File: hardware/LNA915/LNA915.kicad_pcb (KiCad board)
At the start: 4 copper layers, 38 x 7.8 mm, 32 parts, among them P1 HACKRF, P2 ANTENNA, U1 SWITCH, U2 SAW, U3 LNA

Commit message: LNA915 mask clearance fix
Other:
- rule pad_to_mask_clearance: 0.003 -> 0.0762
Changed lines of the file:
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@@
   )
   (setup
-    (last_trace_width 0.24)
+    (last_trace_width 0.1524)
     (user_trace_width 0.2032)
     (user_trace_width 0.24)
@@
     (pad_size 0.762 0.762)
     (pad_drill 0.3048)
-    (pad_to_mask_clearance 0.003)
+    (pad_to_mask_clearance 0.0762)
     (pad_to_paste_clearance_ratio -0.12)
     (aux_axis_origin 0 0)

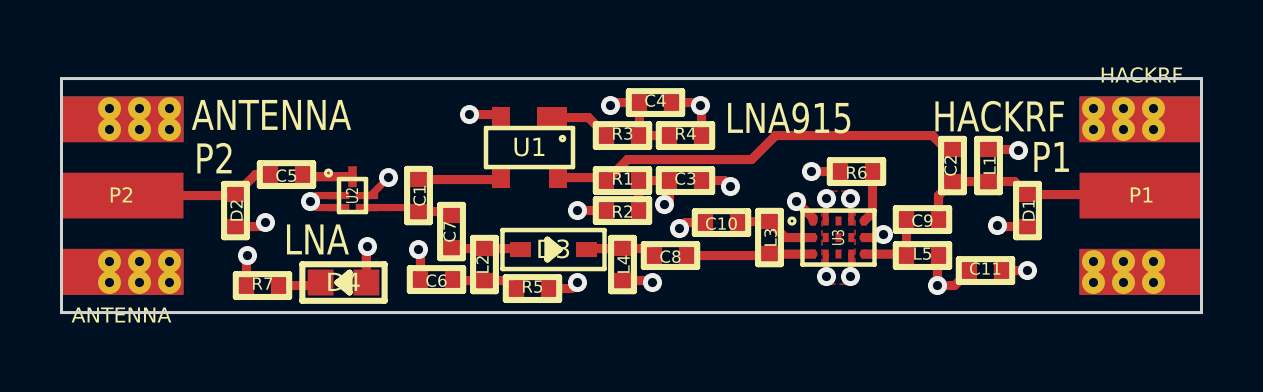
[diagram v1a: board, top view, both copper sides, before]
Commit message: LNA915 grounded mounting holes
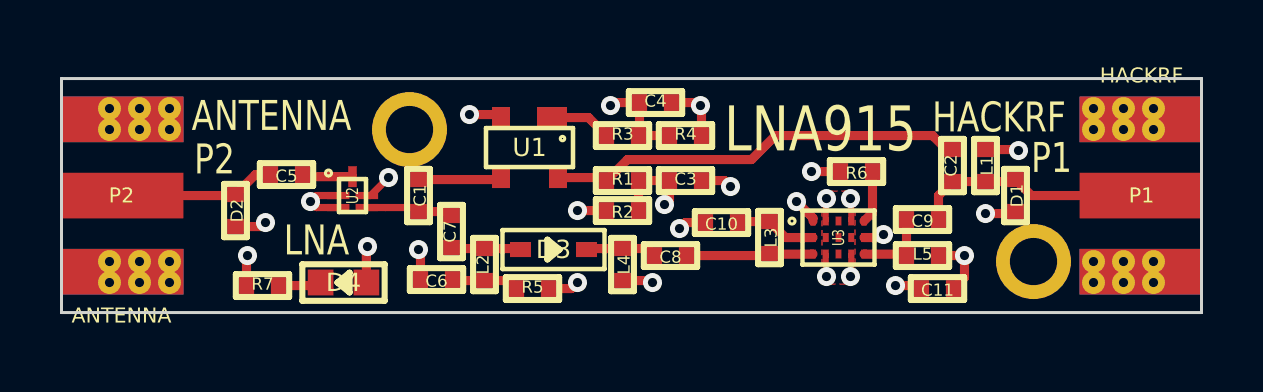
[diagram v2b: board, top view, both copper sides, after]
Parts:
- added P3: CONN_1, GSG-HOLE-62MIL-COPPER, F.Cu at (157.4, 102.2)
- added P4: CONN_1, GSG-HOLE-62MIL-COPPER, F.Cu at (136.6, 97.8)
- moved C11 1.71 mm to (154.2, 103.1), turned to 0 degrees
- moved D1 0.64 mm to (156.8, 100.0)
- moved L1 0.10 mm to (155.8, 99.0)
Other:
- board text added: "9 Feb 2014"
- board text removed: "8 Feb 2014"

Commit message: LNA915 reversed LED orientation to reduce assembly confusion
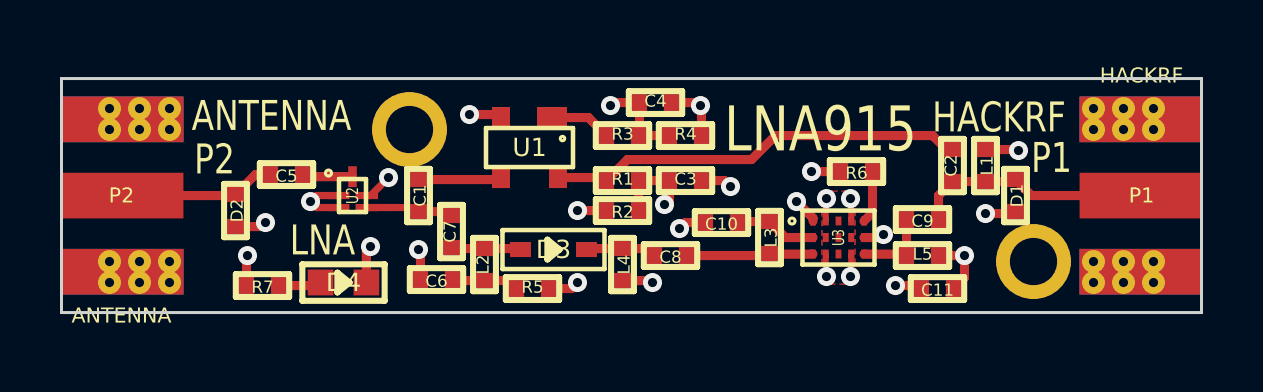
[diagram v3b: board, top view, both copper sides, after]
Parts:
- turned D4 to 0 degrees
- turned R7 to 0 degrees
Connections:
- D4 pad 1: VCC -> N-000009
- D4 pad 2: N-0000015 (its old number) -> GND
- R7 pad 1: N-0000015 (its old number) -> VCC
- R7 pad 2: GND -> N-000009
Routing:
- net N-000009: track 0.00 -> 1.45 mm
- net N-0000015 (its old number): track 1.45 -> 0.00 mm
